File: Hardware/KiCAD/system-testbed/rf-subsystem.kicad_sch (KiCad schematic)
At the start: 33 parts, among them P3 SMA, U10 SKY13278-313, U11 SKY13278-313, U12 SKY13278-313, U13 SN74LVC2G14DBV, U3 CC1200RHBR, U4 SKY13278-313, U6 SKY13278-313, U7 SKY13278-313, X1 40 MHz

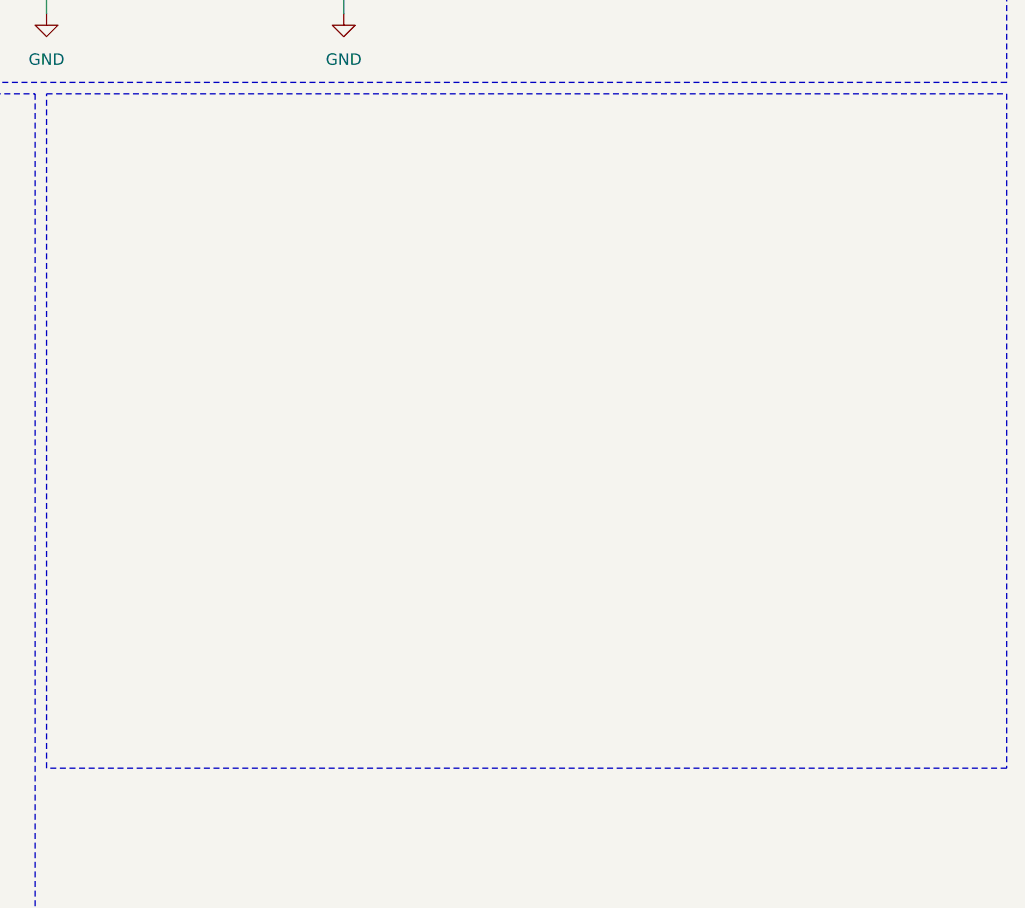
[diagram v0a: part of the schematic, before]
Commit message: fix: create real EYESPI FPC connector symbol and footprint #57
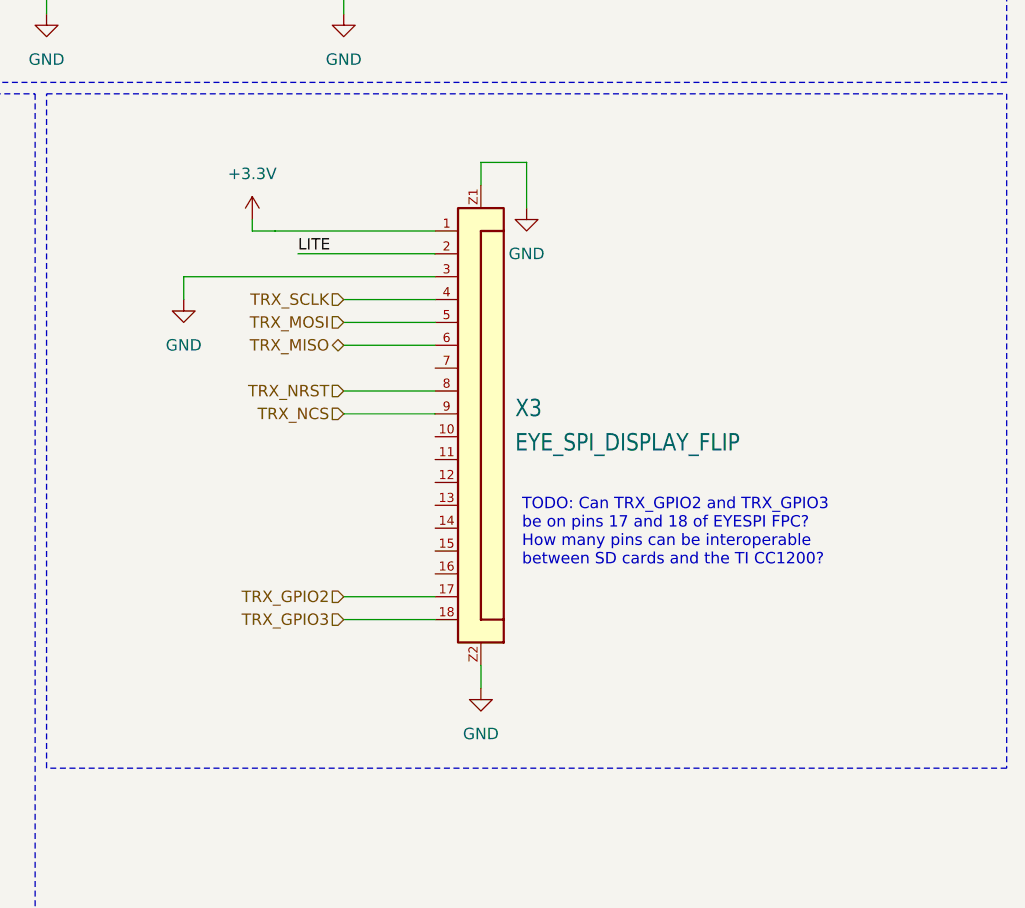
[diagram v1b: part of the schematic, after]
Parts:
- added X3: EYE_SPI_DISPLAY_FLIP, capstone-project:Adafruit EYESPI FPC Connector, symbol capstone-project:Adafruit EYESPI FPC Connector
- C121, C13, C131, C151, C211, C221, C231, C251, C261, C271, C281, C291, C301, C311, C51, C61: footprint Capacitor_SMD:C_0402_1005Metric -> Capacitor_SMD:C_0603_1608Metric
- C37, C5, C6, C7, C8: footprint (none) -> Capacitor_SMD:C_0603_1608Metric
- R12, R141: footprint Resistor_SMD:R_0402_1005Metric -> Resistor_SMD:R_0603_1608Metric
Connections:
- net +3.3V: now also X3.1
- net GND: now also X3.3, X3.Z1, X3.Z2
- net RFSW_{TRX}: now also X3.18
- net TRX_GPIO2: now also X3.17
- net TRX_MISO: now also X3.6
- net TRX_MOSI: now also X3.5
- net TRX_NCS: now also X3.9
- net TRX_NRST: now also X3.8
- net TRX_SCLK: now also X3.4
- new net LITE: X3.2
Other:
- note added: "TODO: Can TRX_GPIO2 and TRX_GPIO3 be on pins 17 and 18 of EYESPI FPC? How many pins can be interoperable between SD cards and the TI CC1200?"

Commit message: fix: relabel TRX GPIOs to breakout over EYESPI #34 #65
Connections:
- net RFSW_{TRX}: no longer X3.18
- net TRX_GPIO0: now also X3.17
- net TRX_GPIO2: now also X3.18; no longer X3.17
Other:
- note added: "TODO: Can TRX_GPIO0 and TRX_GPIO2 be on pins 17 and 18 of EYESPI FPC? How many pins can be interoperable between SD cards and the TI CC1200?"
- note removed: "TODO: Can TRX_GPIO2 and TRX_GPIO3 be on pins 17 and 18 of EYESPI FPC? How many pins can be interoperable between SD cards and the TI CC1200?"
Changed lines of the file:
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@@
 		)
 	)
-	(text "TODO: Can TRX_GPIO2 and TRX_GPIO3\nbe on pins 17 and 18 of EYESPI FPC?\nHow many pins can be interoperable\nbetween SD cards and the TI CC1200?"
+	(text "TODO: Can TRX_GPIO0 and TRX_GPIO2\nbe on pins 17 and 18 of EYESPI FPC?\nHow many pins can be interoperable\nbetween SD cards and the TI CC1200?"
 		(exclude_from_sim no)
 		(at 229.362 133.858 0)
@@
 	(wire
 		(pts
-			(xy 199.39 102.87) (xy 199.39 104.14)
+			(xy 191.77 101.6) (xy 191.77 104.14)
 		)
 		(stroke
@@
 	(wire
 		(pts
-			(xy 199.39 104.14) (xy 201.93 104.14)
+			(xy 191.77 104.14) (xy 201.93 104.14)
 		)
 		(stroke
@@
 		)
 	)
-	(hierarchical_label "TRX_GPIO3"
+	(hierarchical_label "TRX_GPIO2"
 		(shape input)
 		(at 209.55 147.32 180)
@@
 		)
 	)
-	(hierarchical_label "TRX_GPIO2"
+	(hierarchical_label "TRX_GPIO0"
 		(shape input)
 		(at 209.55 144.78 180)
@@
 	(symbol
 		(lib_id "power:+3.3V")
-		(at 199.39 102.87 0)
+		(at 191.77 101.6 0)
 		(unit 1)
 		(exclude_from_sim no)
@@
 		(fields_autoplaced yes)
 		(property "Reference" "#PWR051"
-			(at 199.39 106.68 0)
+			(at 191.77 105.41 0)
 			(effects
 				(font
@@
 		)
 		(property "Value" "+3.3V"
-			(at 199.39 97.79 0)
+			(at 191.77 96.52 0)
 			(effects
 				(font
@@
 		)
 		(property "Footprint" ""
-			(at 199.39 102.87 0)
+			(at 191.77 101.6 0)
 			(effects
 				(font
@@
 		)
 		(property "Datasheet" ""
-			(at 199.39 102.87 0)
+			(at 191.77 101.6 0)
 			(effects
 				(font
@@
 		)
 		(property "Description" "Power symbol creates a global label with name \"+3.3V\""
-			(at 199.39 102.87 0)
+			(at 191.77 101.6 0)
 			(effects
 				(font

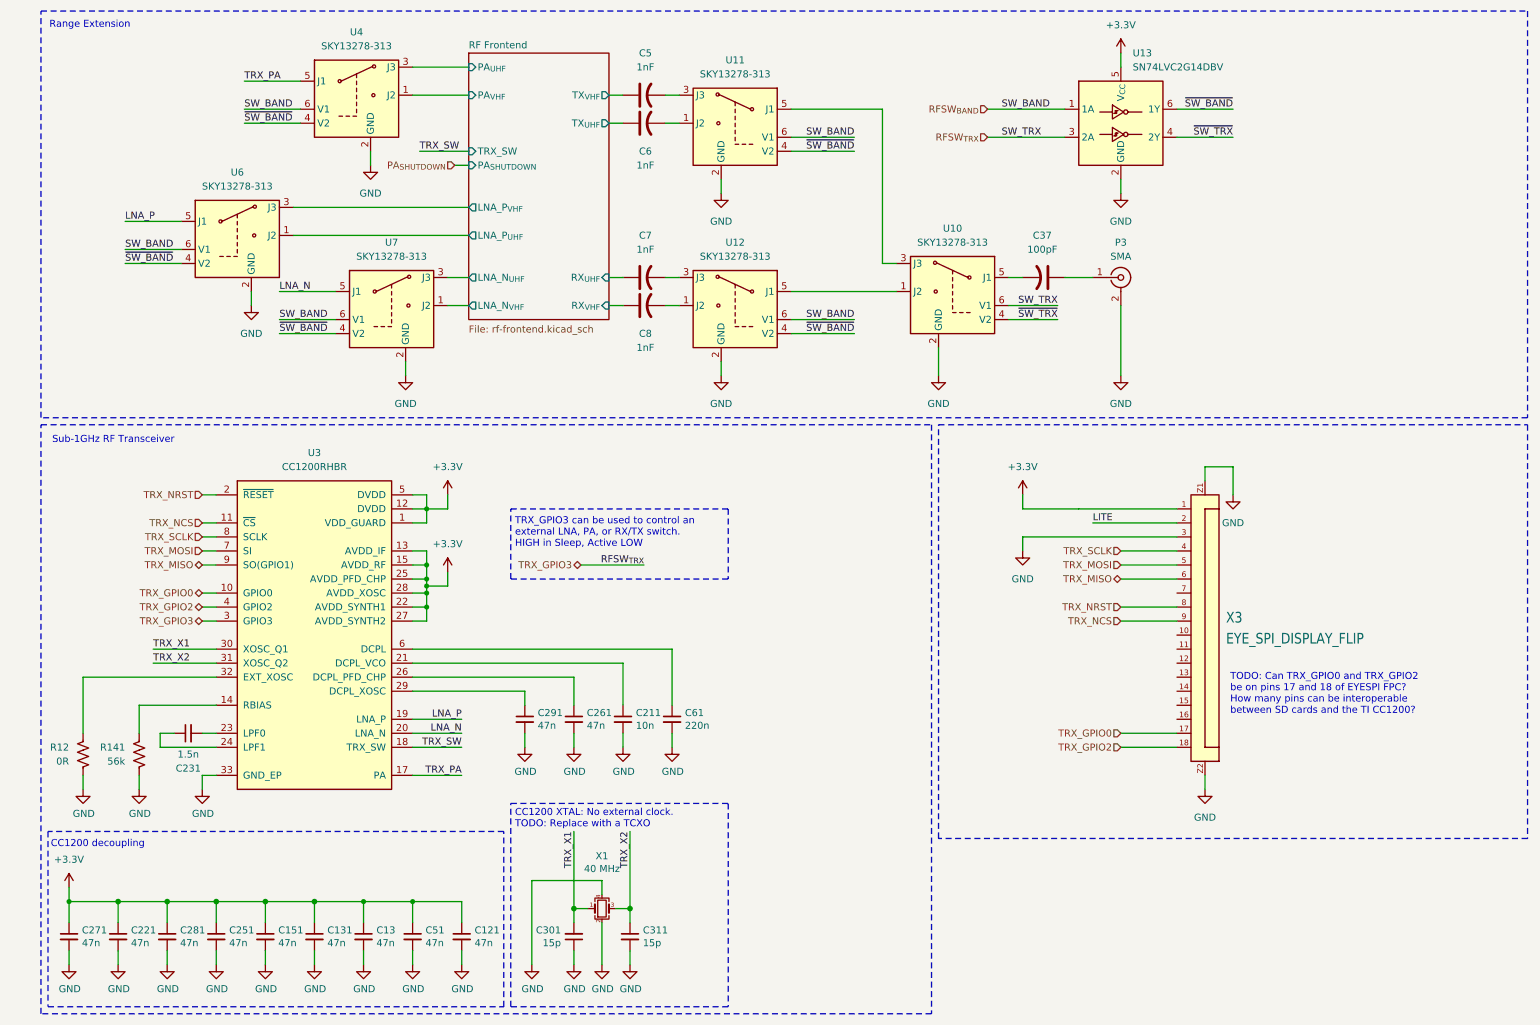
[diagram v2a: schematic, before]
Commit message: feat: begin use of discrete diplexers over band select switches #65 feat: redraw rx/tx switching with built-in decode plus level shifting #34 feat: begin RF modulino testpoints #45
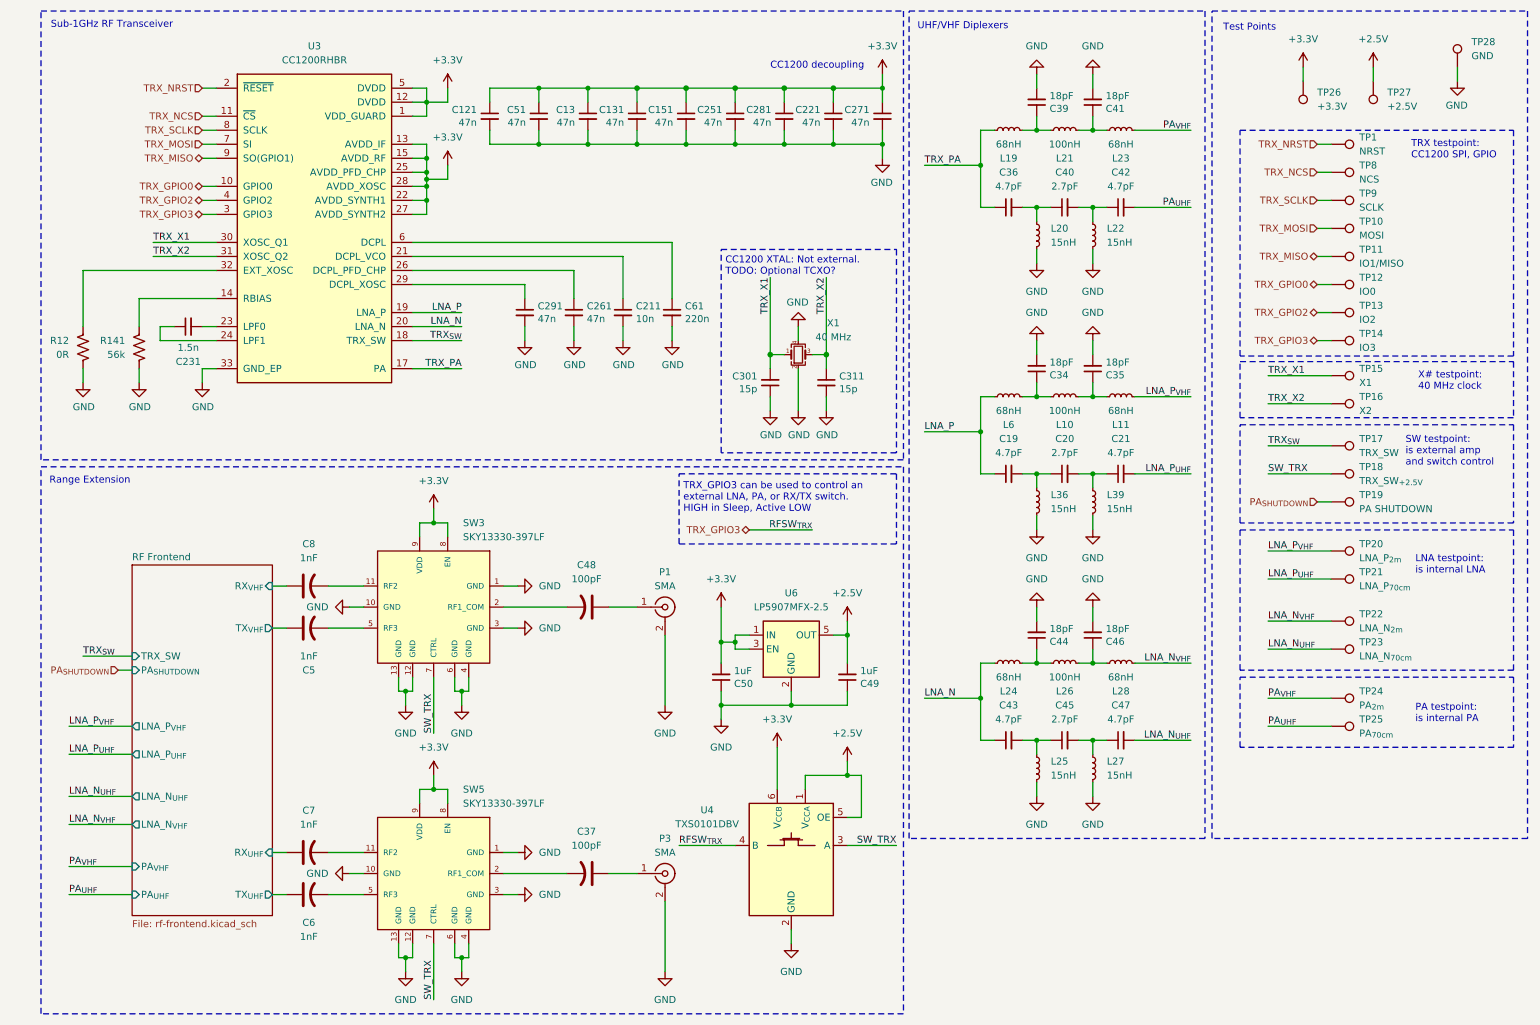
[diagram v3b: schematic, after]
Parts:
- removed U10, U11, U12, U4, U6, U7: SKY13278-313, symbol capstone-project:SKY13278-313
- removed U13: SN74LVC2G14DBV, Package_TO_SOT_SMD:SOT-23-6, symbol 74xGxx:SN74LVC2G14DBV
- removed X3: EYE_SPI_DISPLAY_FLIP, capstone-project:Adafruit EYESPI FPC Connector, symbol capstone-project:Adafruit EYESPI FPC Connector
- added C19, C21, C36, C42, C43, C47: 4.7pF, symbol Device:C_Small
- added C20, C40, C45: 2.7pF, symbol Device:C_Small
- added C34, C35, C39, C41, C44, C46: 18pF, Capacitor_SMD:C_0603_1608Metric, symbol Device:C_Small
- added C48: 100pF, Capacitor_SMD:C_0603_1608Metric, symbol Device:C_US
- added C49, C50: 1uF, Capacitor_SMD:C_0603_1608Metric, symbol Device:C_Small
- added L10, L21, L26: 100nH, symbol Device:L_Small
- added L11, L19, L23, L24, L28, L6: 68nH, symbol Device:L_Small
- added L20, L22, L25, L27, L36, L39: 15nH, Capacitor_SMD:C_0603_1608Metric, symbol Device:L_Small
- added P1: SMA, Connector_Coaxial:SMA_Amphenol_901-143_Horizontal, symbol Connector:Conn_Coaxial
- added SW3, SW5: SKY13330-397LF, SKY13330-397LF:SKY13330-397LF, symbol capstone-project:SKY13330-397LF
- added TP1: NRST, symbol Connector:TestPoint
- added TP10: MOSI, symbol Connector:TestPoint
- added TP11: IO1/MISO, symbol Connector:TestPoint
- added TP12: IO0, symbol Connector:TestPoint
- added TP13: IO2, symbol Connector:TestPoint
- added TP14: IO3, symbol Connector:TestPoint
- added TP15: X1, symbol Connector:TestPoint
- added TP16: X2, symbol Connector:TestPoint
- added TP17: TRX_SW, symbol Connector:TestPoint
- added TP18: TRX_SW_{+2.5V}, symbol Connector:TestPoint
- added TP19: PA SHUTDOWN, symbol Connector:TestPoint
- added TP20: LNA_P_{2m}, symbol Connector:TestPoint
- added TP21: LNA_P_{70cm}, symbol Connector:TestPoint
- added TP22: LNA_N_{2m}, symbol Connector:TestPoint
- added TP23: LNA_N_{70cm}, symbol Connector:TestPoint
- added TP24: PA_{2m}, symbol Connector:TestPoint
- added TP25: PA_{70cm}, symbol Connector:TestPoint
- added TP26: +3.3V, symbol Connector:TestPoint
- added TP27: +2.5V, symbol Connector:TestPoint
- added TP28: GND, symbol Connector:TestPoint
- added TP8: NCS, symbol Connector:TestPoint
- added TP9: SCLK, symbol Connector:TestPoint
- added U4: TXS0101DBV, Package_TO_SOT_SMD:SOT-23-6, symbol Logic_LevelTranslator:TXS0101DBV
- added U6: LP5907MFX-2.5, Package_TO_SOT_SMD:SOT-23-5, symbol Regulator_Linear:LP5907MFX-2.5
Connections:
- net +3.3V: now also C50.2, SW3.8 (EN), SW3.9 (VDD), SW5.8 (EN), SW5.9 (VDD), TP26.1, U4.6 (V_{CCB}), U6.1 (IN), U6.3 (EN)
- net GND: now also C34.2, C35.2, C39.2, C41.2, C44.2, C46.2, C49.1, C50.1, L20.2, L22.2, L25.2, L27.2, L36.2, L39.2, P1.2 (Ext), SW3.1 (GND), SW3.10 (GND), SW3.12 (GND), SW3.13 (GND), SW3.3 (GND), SW3.4 (GND), SW3.6 (GND), SW5.1 (GND), SW5.10 (GND), SW5.12 (GND), SW5.13 (GND), SW5.3 (GND), SW5.4 (GND), SW5.6 (GND), TP28.1, U4.2 (GND), U6.2 (GND)
- net LNA_N: now also C43.1, L24.1
- net LNA_P: now also C19.1, L6.1
- net PA_{SHUTDOWN}: now also TP19.1
- net TRX_GPIO0: now also TP12.1
- net TRX_GPIO2: now also TP13.1
- net TRX_MISO: now also TP11.1
- net TRX_MOSI: now also TP10.1
- net TRX_NCS: now also TP8.1
- net TRX_NRST: now also TP1.1
- net TRX_PA: now also C36.1, L19.1
- net TRX_SCLK: now also TP9.1
- net TRX_X1: now also TP15.1
- net TRX_X2: now also TP16.1
- net at C37.2: now also SW5.2 (RF1_COM)
- net at C5.2: now also SW3.5 (RF3)
- net at C8.2: now also SW3.11 (RF2)
- net at C6.2: now also SW5.5 (RF3)
- net at C7.2: now also SW5.11 (RF2)
- net RFSW_{TRX} renamed TRX_GPIO3
- net TRX_GPIO3: now also TP14.1, U4.4 (B)
- net TRX_SW renamed TRX_{SW}
- net TRX_{SW}: now also TP17.1
- new net: C44.1, L24.2, L26.1
- new net: C19.2, C20.1, L36.1
- new net: C20.2, C21.1, L39.1
- new net: C48.2, SW3.2 (RF1_COM)
- new net: C36.2, C40.1, L20.1
- new net: C40.2, C42.1, L22.1
- new net: C48.1, P1.1 (In)
- new net: C45.2, C47.1, L27.1
- new net: C41.1, L21.2, L23.1
- new net: C39.1, L19.2, L21.1
- new net: C35.1, L10.2, L11.1
- new net: C43.2, C45.1, L25.1
- new net: C46.1, L26.2, L28.1
- new net: C34.1, L10.1, L6.2
- new net +2.5V: C49.2, TP27.1, U4.1 (V_{CCA}), U4.5 (OE), U6.5 (OUT)
- new net LNA_N_{UHF}: C47.2, TP23.1
- new net LNA_N_{VHF}: L28.2, TP22.1
- new net LNA_P_{UHF}: C21.2, TP21.1
- new net LNA_P_{VHF}: L11.2, TP20.1
- new net PA_{UHF}: C42.2, TP25.1
- new net PA_{VHF}: L23.2, TP24.1
- new net SW_TRX: SW3.7 (CTRL), SW5.7 (CTRL), TP18.1, U4.3 (A)
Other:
- note added: "CC1200 XTAL: Not external. TODO: Optional TCXO?"
- note added: "LNA testpoint: is internal LNA"
- note added: "PA testpoint: is internal PA"
- note added: "SW testpoint: is external amp and switch control"
- note added: "TRX testpoint: CC1200 SPI, GPIO"
- note added: "Test Points"
- note added: "UHF/VHF Diplexers"
- note added: "X# testpoint: 40 MHz clock"
- note removed: "CC1200 XTAL: No external clock. TODO: Replace with a TCXO"
- note removed: "TODO: Can TRX_GPIO0 and TRX_GPIO2 be on pins 17 and 18 of EYESPI FPC? How many pins can be interoperable between SD cards and the TI CC1200?"
- moved on the sheet: C121, C13, C131, C151, C211, C221, C231, C251, C261, C271, C281, C291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
